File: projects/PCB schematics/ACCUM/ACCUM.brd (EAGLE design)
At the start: 160 x 100 mm, 14 parts, among them IC2 78L08SMD, Q2 IRLZ44Z

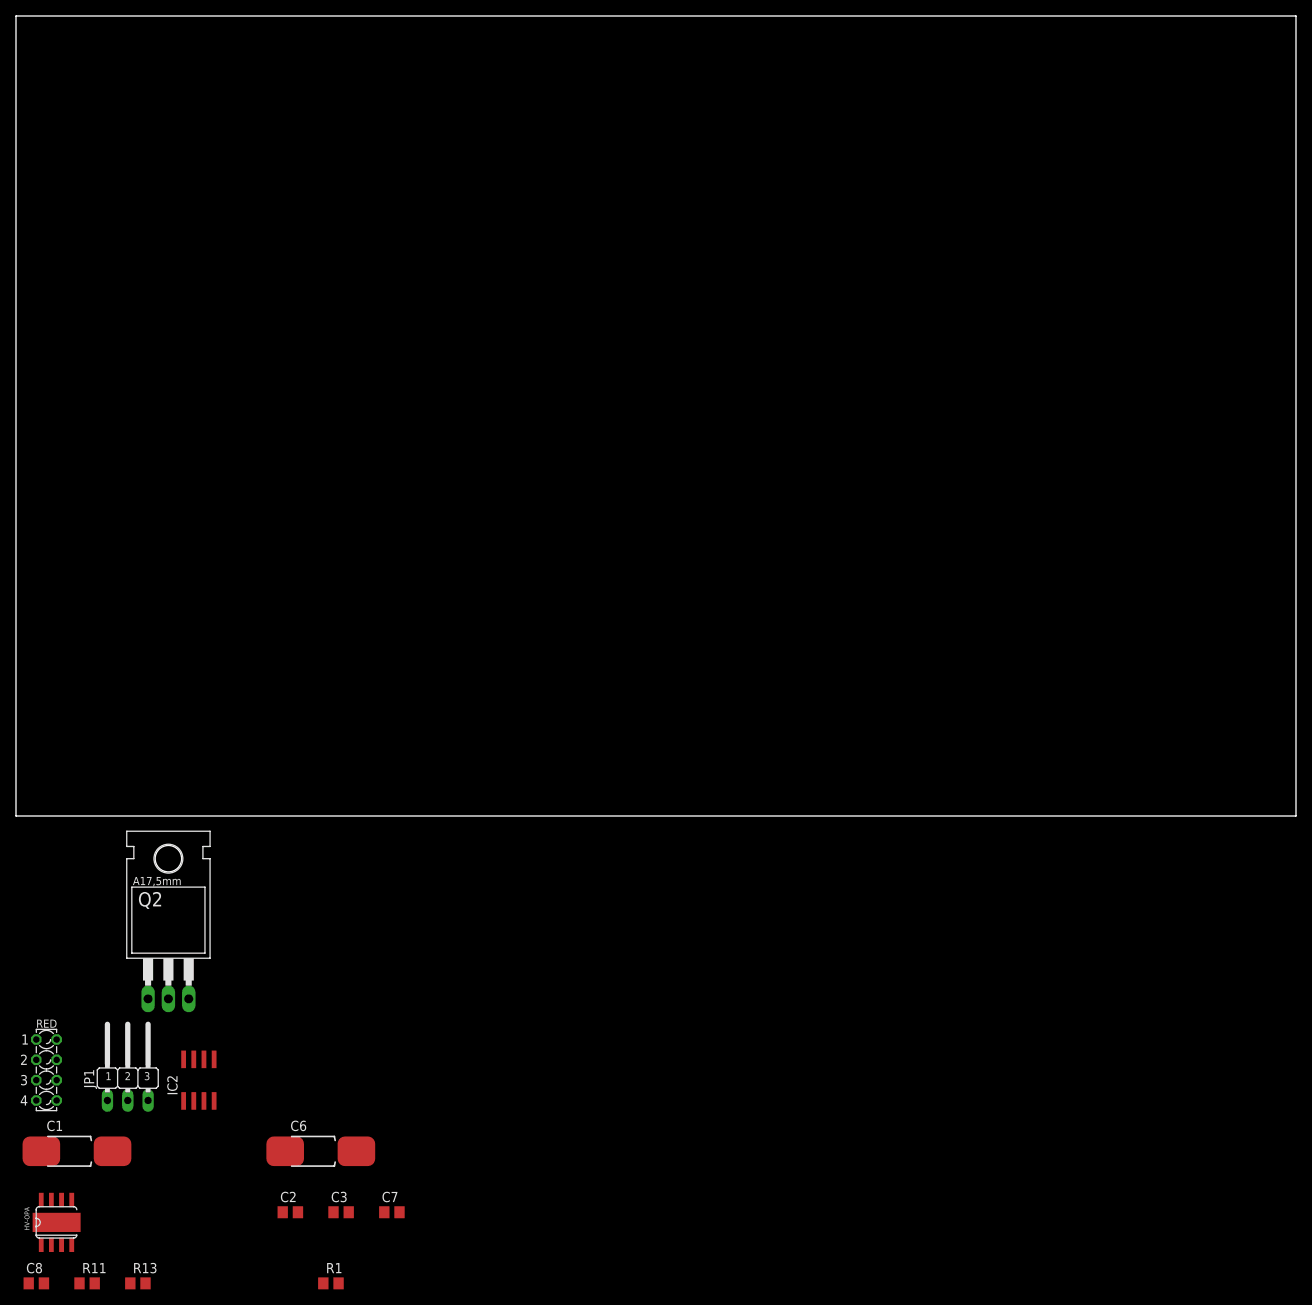
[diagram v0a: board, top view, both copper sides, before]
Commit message: TSMPC - Initial draft (WIP).
Non-working commit of TSMPC.
Done simply to show possible board layout.
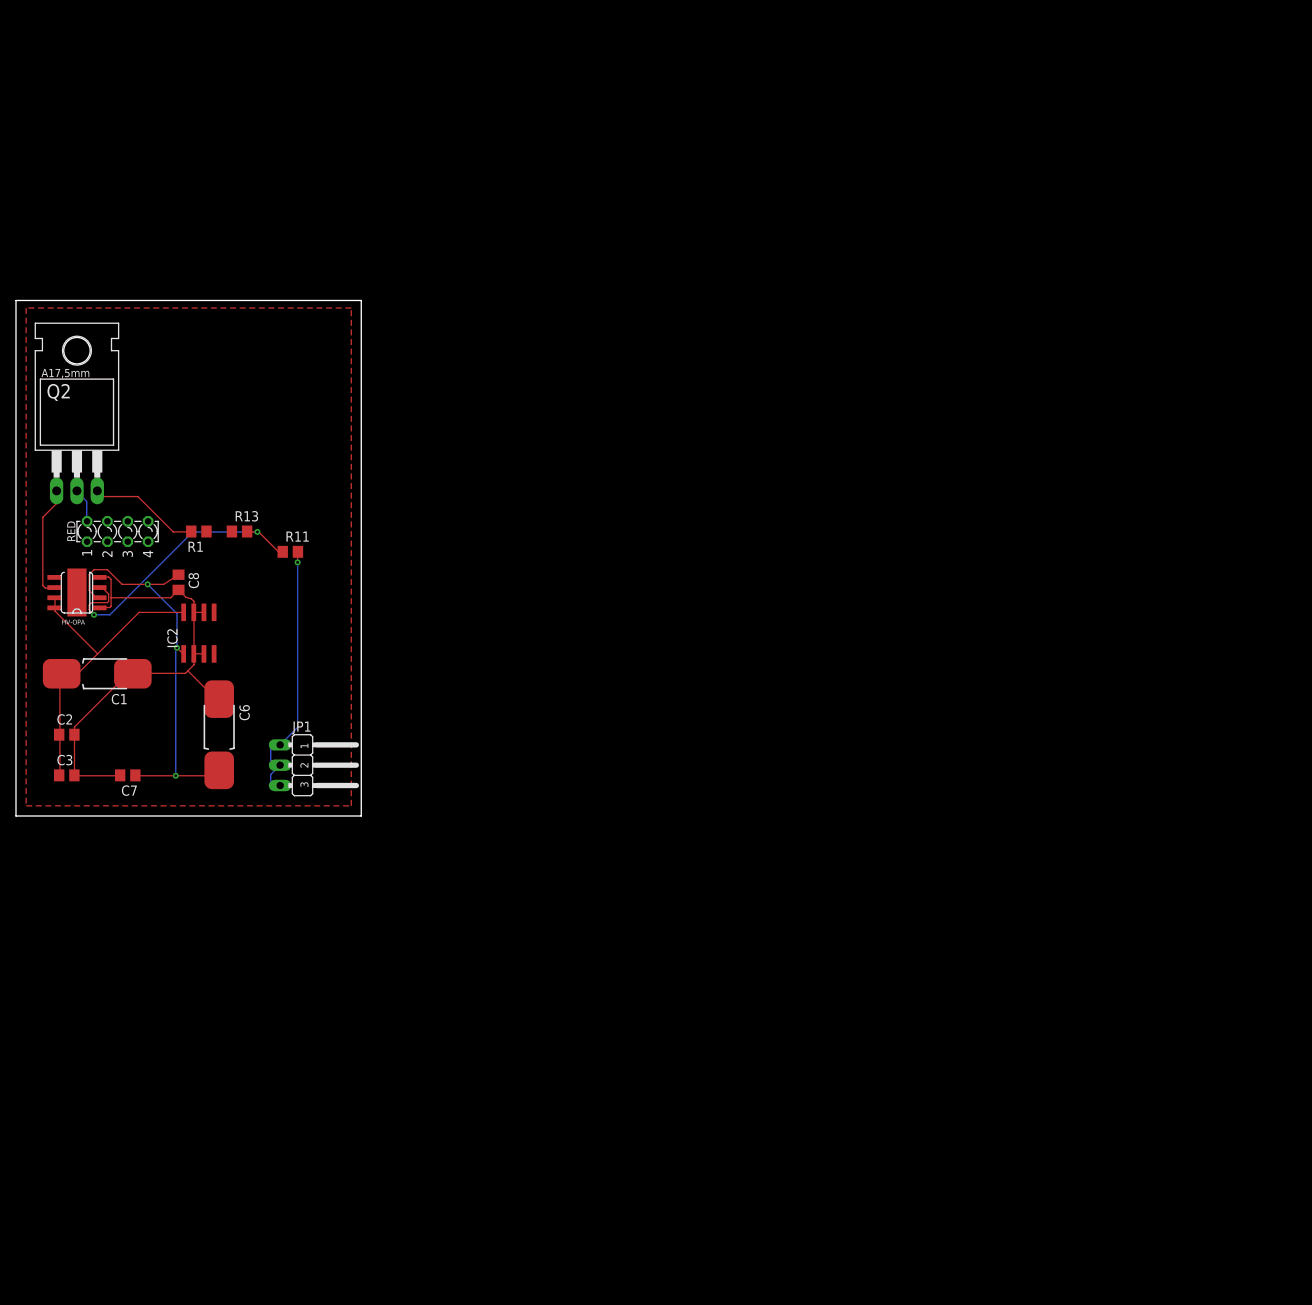
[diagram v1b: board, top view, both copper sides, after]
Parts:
- moved R1 95.4 mm to (22.9, 35.6), turned to 180 degrees
- moved R11 94.9 mm to (34.3, 33.0)
- moved R13 94.8 mm to (27.9, 35.6)
- moved C8 89.4 mm to (20.3, 29.2), turned to 270 degrees
- moved HV-OPA 78.8 mm to (7.62, 27.9), turned to 90 degrees
- moved RED 67.9 mm to (12.7, 35.6), turned to 90 degrees
- moved C2 65.9 mm to (6.35, 10.2)
- moved Q2 64.5 mm to (7.62, 47.0)
- moved C3 64.5 mm to (6.35, 5.08)
- moved C7 63.8 mm to (14.0, 5.08), turned to 180 degrees
- moved C1 59.7 mm to (10.2, 17.8), turned to 180 degrees
- moved IC2 55.9 mm to (22.9, 22.9)
- moved C6 53.6 mm to (25.4, 10.2), turned to 270 degrees
- moved JP1 45.4 mm to (34.3, 6.35), turned to 270 degrees
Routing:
- net HV-: track 0.00 -> 63.7 mm
- net +8V: track 0.00 -> 53.5 mm, vias 0 -> 3
- net V+: track 0.00 -> 40.6 mm
- net VDIV_SIGNAL: track 0.00 -> 36.7 mm, vias 0 -> 2
- net HV_POST_AIR: track 0.00 -> 33.8 mm, vias 0 -> 1
- net +60V-POST-AIR_INDICATOR: track 0.00 -> 14.2 mm
- net N$6: track 0.00 -> 13.9 mm
- net N$2: track 0.00 -> 4.34 mm
- added copper zone on layer 1, net GND
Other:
- board size 160 x 100 mm -> 43.2 x 64.4 mm
